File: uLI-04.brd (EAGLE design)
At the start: 57 x 38.5 mm, 39 parts, among them IC1 PIC18F14K50-I/SS, IC2 ADM2483, IC3 MCP130T, IC4 78L05F, J1 PICPROG2-V, J5 WEBP6, J6 WEBP6, J7 WEBP6, Q1 12.00 MHz, T1 IRF7306, X1 MINI-USB_SHIELD4P-USB-SPEC, X2 ARK1550/2_S

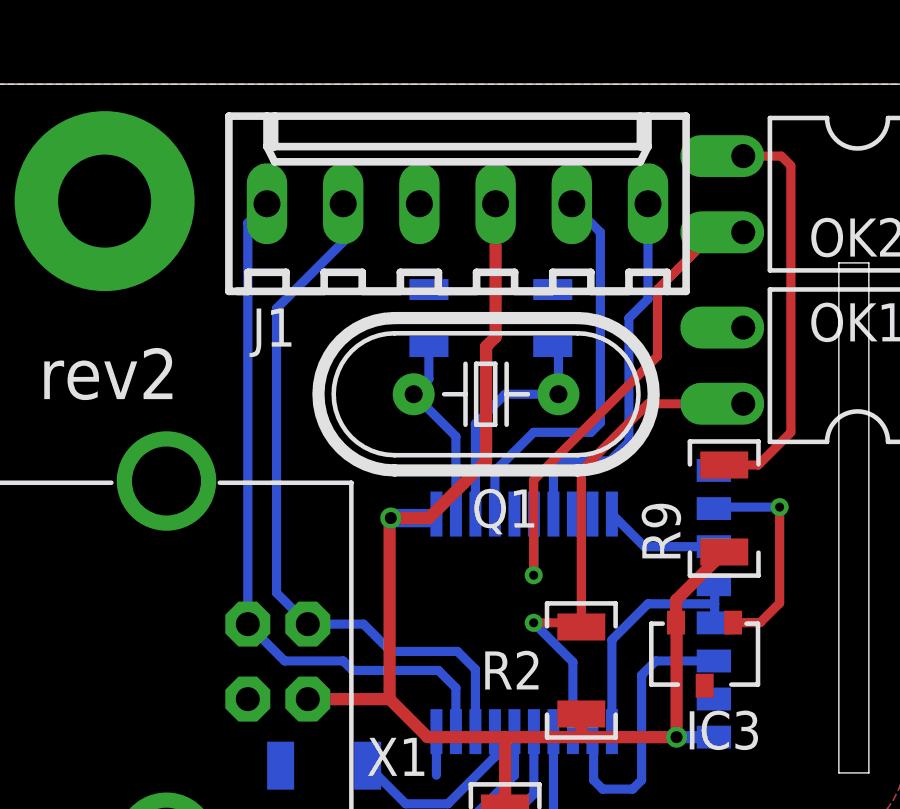
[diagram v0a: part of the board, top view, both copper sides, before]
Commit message: Progrmaovaci konektor posunut o 0.5 mm doleva.
Close #7.
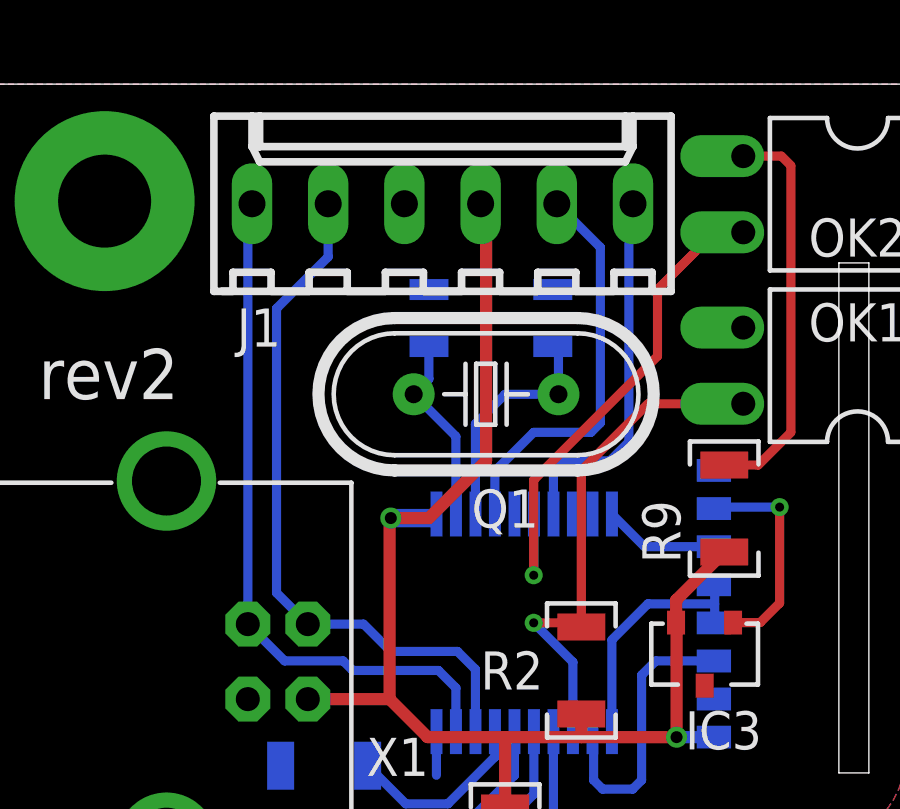
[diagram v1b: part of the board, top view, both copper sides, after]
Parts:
- moved J1 0.50 mm to (17.0, 36.5)
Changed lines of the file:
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@@
 <setting verticaltext="up"/>
 </settings>
-<grid distance="0.5" unitdist="mm" unit="mm" style="dots" multiple="2" display="no" altdistance="0.1" altunitdist="mm" altunit="mm"/>
+<grid distance="0.5" unitdist="mm" unit="mm" style="dots" multiple="2" display="no" altdistance="0.25" altunitdist="mm" altunit="mm"/>
 <layers>
 <layer number="1" name="Top" color="3" fill="1" visible="yes" active="yes"/>
@@
 <attribute name="VALUE" x="19.05" y="22.225" size="1.27" layer="27" font="vector" ratio="15" rot="R270"/>
 </element>
-<element name="J1" library="con-molex" package="6410-06-PICPROG" value="PICPROG2-V" x="17.4625" y="36.5125" smashed="yes">
-<attribute name="NAME" x="11.3425" y="33.02" size="1.27" layer="25" font="vector" ratio="15" rot="R180" align="bottom-center"/>
+<element name="J1" library="con-molex" package="6410-06-PICPROG" value="PICPROG2-V" x="16.9625" y="36.5125" smashed="yes">
+<attribute name="NAME" x="10.8425" y="33.02" size="1.27" layer="25" font="vector" ratio="15" rot="R180" align="bottom-center"/>
 </element>
 <element name="LED4" library="led" package="LED3MM" value="" x="54.9275" y="30.1625" smashed="yes" rot="MR180">
@@
 <wire x1="14.33" y1="22.5" x2="15.24" y2="21.59" width="0.3048" layer="16"/>
 <wire x1="15.24" y1="21.59" x2="17.4625" y2="21.59" width="0.3048" layer="16"/>
-<wire x1="13.6525" y1="36.5125" x2="13.6525" y2="35.2425" width="0.3048" layer="16"/>
-<wire x1="13.6525" y1="35.2425" x2="11.43" y2="33.02" width="0.3048" layer="16"/>
+<wire x1="13.1525" y1="36.5125" x2="13.1525" y2="34.7425" width="0.3048" layer="16"/>
+<wire x1="13.1525" y1="34.7425" x2="11.43" y2="33.02" width="0.3048" layer="16"/>
 <wire x1="11.43" y1="33.02" x2="11.43" y2="23.5425" width="0.3048" layer="16"/>
 <wire x1="11.43" y1="23.5425" x2="12.4725" y2="22.5" width="0.3048" layer="16"/>
@@
 <wire x1="13.6525" y1="21.2725" x2="11.7" y2="21.2725" width="0.3048" layer="16"/>
 <wire x1="11.7" y1="21.2725" x2="10.4725" y2="22.5" width="0.3048" layer="16"/>
-<wire x1="10.4725" y1="22.5" x2="10.4725" y2="35.8725" width="0.3048" layer="16"/>
-<wire x1="10.4725" y1="35.8725" x2="11.1125" y2="36.5125" width="0.3048" layer="16"/>
+<wire x1="10.4725" y1="22.5" x2="10.4725" y2="36.3725" width="0.3048" layer="16"/>
+<wire x1="10.4725" y1="36.3725" x2="10.6125" y2="36.5125" width="0.3048" layer="16"/>
 </signal>
 <signal name="VDD">
@@
 <contactref element="R2" pad="2"/>
 <via x="15.24" y="26.035" extent="1-16" drill="0.4"/>
-<wire x1="18.7325" y1="32.0675" x2="18.415" y2="31.75" width="0.4064" layer="1"/>
-<wire x1="18.415" y1="31.75" x2="18.415" y2="27.94" width="0.4064" layer="1"/>
 <wire x1="18.415" y1="27.94" x2="16.51" y2="26.035" width="0.4064" layer="1"/>
 <wire x1="16.51" y1="26.035" x2="15.24" y2="26.035" width="0.4064" layer="1"/>
@@
 <wire x1="19.05" y1="16.3725" x2="19.05" y2="18.7325" width="0.4064" layer="1"/>
 <contactref element="J1" pad="3"/>
-<wire x1="18.7325" y1="32.0675" x2="18.7325" y2="36.5125" width="0.4064" layer="1"/>
 <contactref element="IC2" pad="1"/>
 <contactref element="R9" pad="2"/>
@@
 <wire x1="24.75" y1="22.55" x2="24.75" y2="23.3" width="0.4064" layer="1"/>
 <wire x1="24.75" y1="23.3" x2="26.3525" y2="24.9025" width="0.4064" layer="1"/>
+<wire x1="18.415" y1="27.94" x2="18.415" y2="36.33" width="0.4064" layer="1"/>
+<wire x1="18.415" y1="36.33" x2="18.2325" y2="36.5125" width="0.4064" layer="1"/>
 </signal>
 <signal name="PROC_RX">
@@
 <wire x1="20.955" y1="27.94" x2="22.5425" y2="27.94" width="0.3048" layer="16"/>
 <wire x1="22.5425" y1="27.94" x2="23.1775" y2="28.575" width="0.3048" layer="16"/>
-<wire x1="23.1775" y1="28.575" x2="23.1775" y2="32.7025" width="0.3048" layer="16"/>
+<wire x1="23.1775" y1="28.575" x2="23.1775" y2="36.3775" width="0.3048" layer="16"/>
 <contactref element="J1" pad="1"/>
-<wire x1="23.8125" y1="36.5125" x2="23.8125" y2="33.3375" width="0.3048" layer="16"/>
-<wire x1="23.8125" y1="33.3375" x2="23.1775" y2="32.7025" width="0.3048" layer="16"/>
+<wire x1="23.1775" y1="36.3775" x2="23.3125" y2="36.5125" width="0.3048" layer="16"/>
 </signal>
 <signal name="!MCLR">
@@
 <wire x1="20.0025" y1="28.8925" x2="21.9075" y2="28.8925" width="0.3048" layer="16"/>
 <wire x1="21.9075" y1="28.8925" x2="22.225" y2="29.21" width="0.3048" layer="16"/>
-<wire x1="22.225" y1="29.21" x2="22.225" y2="35.56" width="0.3048" layer="16"/>
+<wire x1="22.225" y1="29.21" x2="22.225" y2="35.06" width="0.3048" layer="16"/>
 <contactref element="J1" pad="2"/>
-<wire x1="21.2725" y1="36.5125" x2="22.225" y2="35.56" width="0.3048" layer="16"/>
+<wire x1="20.7725" y1="36.5125" x2="22.225" y2="35.06" width="0.3048" layer="16"/>
 </signal>
 <signal name="LED1_R">

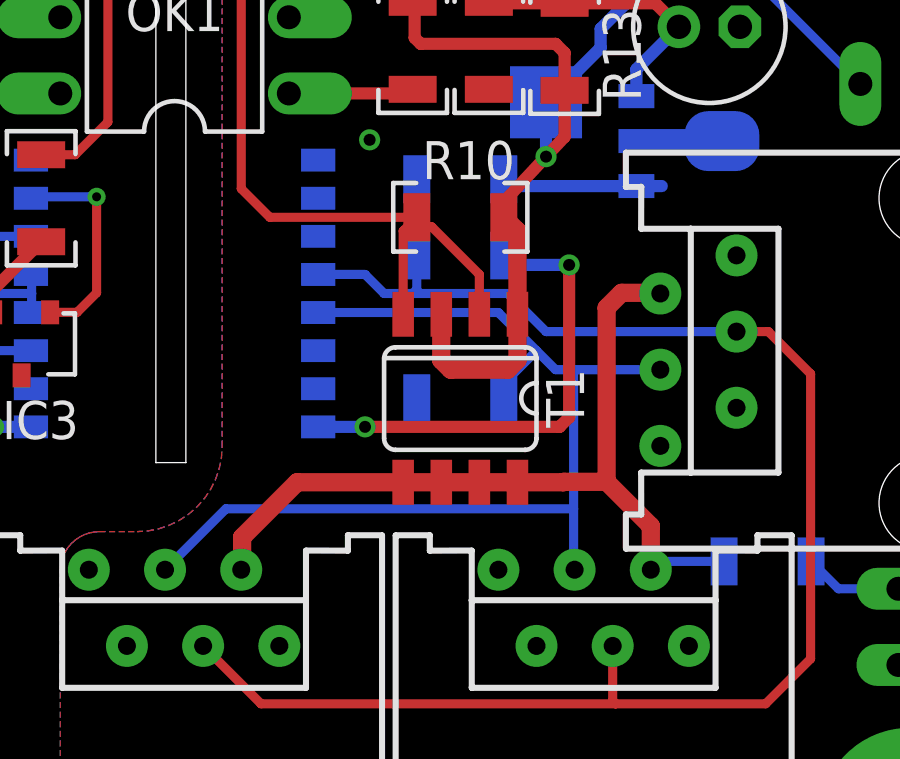
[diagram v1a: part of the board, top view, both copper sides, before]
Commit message: Odstranen kus dratu u stabilizatoru.
Close #6.
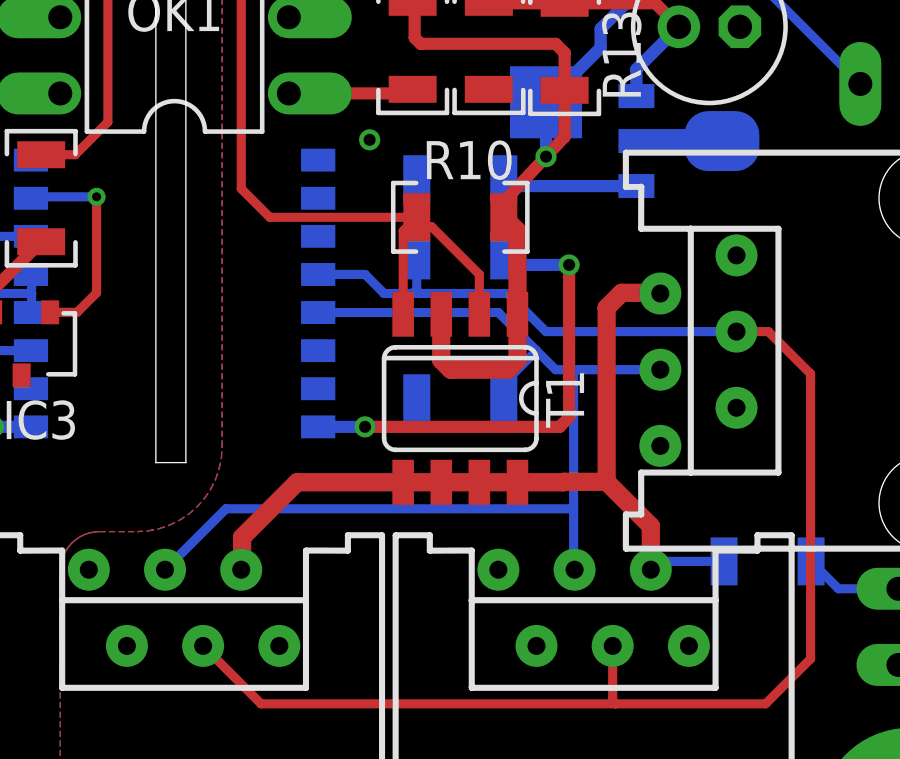
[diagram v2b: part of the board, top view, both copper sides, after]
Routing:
- net VCCINT: track 23.8 -> 22.9 mm
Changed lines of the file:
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@@
 <wire x1="43.95" y1="24.13" x2="42.09" y2="24.13" width="0.4064" layer="16"/>
 <wire x1="42.09" y1="24.13" x2="41.7725" y2="24.4475" width="0.4064" layer="16"/>
-<wire x1="46.1925" y1="26.7575" x2="47.04" y2="26.7575" width="0.4064" layer="16"/>
 </signal>
 <signal name="BUS_A" class="1">
@@
 <wire x1="45.2" y1="16.9" x2="46.6725" y2="15.4275" width="0.6096" layer="1"/>
 <wire x1="46.6725" y1="15.4275" x2="46.6725" y2="13.97" width="0.6096" layer="1"/>
-<wire x1="33.05" y1="14" x2="33.05" y2="15.05" width="0.6096" layer="1"/>
 <wire x1="33.05" y1="15.05" x2="34.885" y2="16.885" width="0.6096" layer="1"/>
 <wire x1="38.4175" y1="16.885" x2="34.885" y2="16.885" width="0.6096" layer="1"/>
 <wire x1="49.115" y1="14.2475" x2="46.95" y2="14.2475" width="0.3048" layer="16"/>
 <wire x1="46.95" y1="14.2475" x2="46.6725" y2="13.97" width="0.3048" layer="16"/>
-<wire x1="33.05" y1="14" x2="33.02" y2="13.97" width="0" layer="19" extent="1-1"/>
+<wire x1="33.05" y1="15.05" x2="33.05" y2="14" width="0.6096" layer="1"/>
+<wire x1="33.05" y1="14" x2="33.02" y2="13.97" width="0.6096" layer="1"/>
 </signal>
 <signal name="N$1" class="1">

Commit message: Posunut C5.
Close $5.
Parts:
- moved C5 6.43 mm to (18.8, 14.9), flipped to the top, turned to 270 degrees
- moved C4 2.50 mm to (21.6, 14.9)
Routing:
- net VBUS: track 6.26 -> 6.04 mm, vias 0 -> 1
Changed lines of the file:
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@@
 </autorouter>
 <elements>
-<element name="C5" library="rcl" package="C1206" value="470n" x="13.0175" y="17.78" smashed="yes" rot="MR0">
-<attribute name="NAME" x="10.3875" y="17.35" size="1.27" layer="26" font="vector" ratio="15" rot="MR0"/>
-<attribute name="VALUE" x="9.7875" y="17.24" size="1.27" layer="28" font="vector" ratio="15" rot="MR0"/>
-</element>
-<element name="C4" library="rcl" package="C1206" value="100n" x="19.05" y="14.9225" smashed="yes" rot="R270">
-<attribute name="NAME" x="20.6375" y="14.605" size="1.27" layer="25" font="vector" ratio="15"/>
-<attribute name="VALUE" x="16.51" y="16.1925" size="1.27" layer="27" font="vector" ratio="15" rot="R270"/>
+<element name="C5" library="rcl" package="C1206" value="470n" x="18.78" y="14.9225" smashed="yes" rot="R270">
+<attribute name="NAME" x="18.35" y="12.2925" size="1.27" layer="25" font="vector" ratio="15" rot="R270"/>
+<attribute name="VALUE" x="18.24" y="11.6925" size="1.27" layer="27" font="vector" ratio="15" rot="R270"/>
+</element>
+<element name="C4" library="rcl" package="C1206" value="100n" x="21.55" y="14.9225" smashed="yes" rot="R270">
+<attribute name="NAME" x="23.1375" y="14.605" size="1.27" layer="25" font="vector" ratio="15"/>
+<attribute name="VALUE" x="19.01" y="16.1925" size="1.27" layer="27" font="vector" ratio="15" rot="R270"/>
 </element>
 <element name="C8" library="rcl" package="C1206" value="100n" x="40.3225" y="26.9875" smashed="yes" rot="MR0">
@@
 <wire x1="18.71" y1="18.9175" x2="18.71" y2="18.075" width="0.3048" layer="16"/>
 <wire x1="18.71" y1="18.075" x2="17.145" y2="16.51" width="0.3048" layer="16"/>
-<wire x1="17.145" y1="16.51" x2="15.7375" y2="16.51" width="0.3048" layer="16"/>
-<wire x1="15.7375" y1="16.51" x2="14.4675" y2="17.78" width="0.3048" layer="16"/>
+<via x="16.5" y="16.5" extent="1-16" drill="0.3"/>
+<wire x1="16.5" y1="16.5" x2="18.6525" y2="16.5" width="0.3048" layer="1"/>
+<wire x1="18.6525" y1="16.5" x2="18.78" y2="16.3725" width="0.3048" layer="1"/>
+<wire x1="17.145" y1="16.51" x2="16.51" y2="16.51" width="0.3048" layer="16"/>
+<wire x1="16.51" y1="16.51" x2="16.5" y2="16.5" width="0.3048" layer="16"/>
 </signal>
 <signal name="USB_D-">
@@
 <via x="24.765" y="18.7325" extent="1-16" drill="0.4"/>
 <wire x1="24.765" y1="18.7325" x2="21.59" y2="18.7325" width="0.4064" layer="1"/>
-<wire x1="21.59" y1="18.7325" x2="19.05" y2="18.7325" width="0.4064" layer="1"/>
+<wire x1="21.59" y1="18.7325" x2="21.55" y2="18.7325" width="0.4064" layer="1"/>
 <wire x1="21.59" y1="19.505" x2="21.59" y2="18.7325" width="0.4064" layer="1"/>
-<wire x1="19.05" y1="16.3725" x2="19.05" y2="18.7325" width="0.4064" layer="1"/>
+<wire x1="21.55" y1="16.3725" x2="21.55" y2="18.7325" width="0.4064" layer="1"/>
 <contactref element="J1" pad="3"/>
 <contactref element="IC2" pad="1"/>
 <contactref element="R9" pad="2"/>
 <contactref element="X1" pad="1"/>
-<wire x1="19.05" y1="18.7325" x2="16.4675" y2="18.7325" width="0.4064" layer="1"/>
+<wire x1="21.55" y1="18.7325" x2="16.4675" y2="18.7325" width="0.4064" layer="1"/>
 <wire x1="12.4725" y1="20" x2="15.2" y2="20" width="0.4064" layer="1"/>
 <wire x1="15.2" y1="20" x2="15.2" y2="25.995" width="0.4064" layer="1"/>
